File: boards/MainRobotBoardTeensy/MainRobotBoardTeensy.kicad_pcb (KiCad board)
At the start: 2 copper layers, 109.6 x 129.9 mm, 108 parts, among them J1 IDC, J10 B3B-XH-A, J11 B3B-XH-A, J12 B3B-XH-A, J13 B3B-XH-A, J14 IDC, J15 IDC, J16 IDC, J2 B3B-XH-A, J3 B3B-XH-A, J4 B3B-XH-A, J5 B3B-XH-A, J6 B3B-XH-A, J7 B3B-XH-A, J8 B3B-XH-A, J9 B3B-XH-A, Q1 MMBT3904LT1G, Q10 MMBT3904LT1G, Q11 MMBT3904LT1G, Q12 MMBT3904LT1G, Q13 MMBT3904LT1G, Q14 MMBT3904LT1G, Q15 MMBT3904LT1G, Q16 MMBT3904LT1G, Q17 MMBT3904LT1G, Q18 MMBT3904LT1G, Q19 MMBT3904LT1G, Q2 MMBT3904LT1G, Q20 MMBT3904LT1G, Q21 MMBT3904LT1G, Q22 MMBT3904LT1G, Q23 MMBT3904LT1G, Q24 MMBT3904LT1G, Q3 MMBT3904LT1G, Q4 MMBT3904LT1G, Q5 MMBT3904LT1G, Q6 MMBT3904LT1G, Q7 MMBT3904LT1G, Q8 MMBT3904LT1G, Q9 MMBT3904LT1G, U1 Teensy4.0, U2 TLC555CDR, U3 SN74HC08DR, U4 SN74HC08DR, U5 PCA9685PW_118, U6 SN74HC08DR, U7 SN74HC08DR, U8 BNO055

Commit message: Update main and leg board
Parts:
- removed D21, D22, D23, D24: BLUELED, 150080BS75000:150080BS75000_Modified
- removed J15, J16: IDC, Connector_IDC:IDC-Header_2x04_P2.54mm_Vertical
- removed Q21, Q22, Q23, Q24: MMBT3904LT1G, SMMBT3904LT1G:MMBT3904LT1G
- removed U5: PCA9685PW_118, PCA9685PW,118:PCA9685PW,118
- removed U7: SN74HC08DR, SN74HC08DR:SN74HC08DR
- removed U8: BNO055, BNO055:BNO055
- added C5: 47nF, Capacitor47nF:CAPC1608X90N, F.Cu at (110.9, 134.8)
- added C6: 47nF, Capacitor47nF:CAPC1608X90N, F.Cu at (110.9, 137.5)
- added R29: 47R, Resistor47:RESC1608X55, F.Cu at (147.3, 98.9)
- added R30: 47R, Resistor47:RESC1608X55, F.Cu at (141.1, 98.9)
- added R31: 47R, Resistor47:RESC1608X55, F.Cu at (152.6, 105.0)
- added R32: 47R, Resistor47:RESC1608X55, F.Cu at (115.5, 147.5)
- added R33: 47R, Resistor47:RESC1608X55, F.Cu at (152.6, 125.8)
- added R34: 2.2K, Resistor2.2K:RC0603FR-072K2L, F.Cu at (115.4, 129.1)
- added R35: 2.2K, Resistor2.2K:RC0603FR-072K2L, F.Cu at (115.4, 132.0)
- added R36: 2.2K, Resistor2.2K:RC0603FR-072K2L, F.Cu at (115.4, 134.8)
- added R37: 2.2K, Resistor2.2K:RC0603FR-072K2L, F.Cu at (115.4, 137.5)
- added R38: 10K, Resistor10K:CRCW060310K0FKEA, F.Cu at (147.4, 52.3)
- added R39: 10K, Resistor10K:CRCW060310K0FKEA, F.Cu at (152.9, 54.9)
- added R40: 10K, Resistor10K:CRCW060310K0FKEA, F.Cu at (152.9, 70.7)
- added R41: 10K, Resistor10K:CRCW060310K0FKEA, F.Cu at (147.4, 68.1)
- added R42: 10K, Resistor10K:CRCW060310K0FKEA, F.Cu at (152.9, 85.2)
- added R43: 10K, Resistor10K:CRCW060310K0FKEA, F.Cu at (147.4, 81.9)
- added R44: 10K, Resistor10K:CRCW060310K0FKEA, F.Cu at (152.7, 98.9)
- added R45: 10K, Resistor10K:CRCW060310K0FKEA, F.Cu at (141.3, 96.1)
- added R46: 10K, Resistor10K:CRCW060310K0FKEA, F.Cu at (152.7, 107.7)
- added R47: 10K, Resistor10K:CRCW060310K0FKEA, F.Cu at (115.4, 150.1)
- added R48: 10K, Resistor10K:CRCW060310K0FKEA, F.Cu at (141.3, 122.9)
- added R49: 10K, Resistor10K:CRCW060310K0FKEA, F.Cu at (146.7, 143.6)
- added R50: 10K, Resistor10K:CRCW060310K0FKEA, F.Cu at (141.3, 52.3)
- added R51: 10K, Resistor10K:CRCW060310K0FKEA, F.Cu at (141.3, 68.1)
- added R52: 10K, Resistor10K:CRCW060310K0FKEA, F.Cu at (141.3, 82.2)
- added R53: 10K, Resistor10K:CRCW060310K0FKEA, F.Cu at (147.4, 96.1)
- added R54: 10K, Resistor10K:CRCW060310K0FKEA, F.Cu at (95.4, 110.0)
- added R55: 10K, Resistor10K:CRCW060310K0FKEA, F.Cu at (95.4, 134.1)
- added R56: 47R, Resistor47:RESC1608X55, F.Cu at (115.5, 126.4)
- added R57: 47R, Resistor47:RESC1608X55, F.Cu at (141.1, 125.8)
- C1: footprint CC0603JRX7R7BB105:CC0603JRX7R7BB105 -> Capacitor1uF:CC0603JRX7R7BB105
- C2: footprint C0402C103J4RACTU:C0402C103J4RACTU -> Capacitor0.01uF:C0402C103J4RACTU
- C3: value 1uF -> 47nF; footprint CC0603JRX7R7BB105:CC0603JRX7R7BB105 -> Capacitor47nF:CAPC1608X90N
- C4: value 100nF -> 47nF; footprint CC0603KRX7R9BB104:CC0603KRX7R9BB104 -> Capacitor47nF:CAPC1608X90N
- D1, D2, D3, D4, D5, D6, D7, D8: footprint NCD0603R1:NCD0603R1 -> LedRed:NCD0603R1
- D10, D11, D12, D13, D14, D15, D16, D17, D18, D19, D20, D9: footprint 150080BS75000:150080BS75000_Modified -> LedBlue:150080BS75000_Modified
- J1: value IDC -> B3B-XH-A; footprint Connector_IDC:IDC-Header_2x04_P2.54mm_Vertical -> Connector_JST:JST_XH_B3B-XH-A_1x03_P2.50mm_Vertical
- J10, J12: value B3B-XH-A -> B4B-XH-A; footprint Connector_JST:JST_XH_B3B-XH-A_1x03_P2.50mm_Vertical -> Connector_JST:JST_XH_B4B-XH-A_1x04_P2.50mm_Vertical
- J11: value B3B-XH-A -> IDC; footprint Connector_JST:JST_XH_B3B-XH-A_1x03_P2.50mm_Vertical -> Connector_IDC:IDC-Header_2x04_P2.54mm_Vertical
- J13: value B3B-XH-A -> B5B-XH-A; footprint Connector_JST:JST_XH_B3B-XH-A_1x03_P2.50mm_Vertical -> Connector_JST:JST_XH_B5B-XH-A_1x05_P2.50mm_Vertical
- J14: value IDC -> B5B-XH-A; footprint Connector_IDC:IDC-Header_2x04_P2.54mm_Vertical -> Connector_JST:JST_XH_B5B-XH-A_1x05_P2.50mm_Vertical
- Q1, Q10, Q11, Q12, Q13, Q14, Q15, Q16, Q17, Q18, Q19, Q2, Q20, Q3, Q4, Q5, Q6, Q7, Q8, Q9: footprint SMMBT3904LT1G:MMBT3904LT1G -> Transistor:MMBT3904LT1G
- R1: footprint RC0603FR-07360KL:RC0603FR-07360KL -> Resistor360K:RC0603FR-07360KL
- R10, R3, R4, R5, R6, R7, R8, R9: footprint RCG06031K00FKEA:RCG06031K00FKEA -> Resistor1K:RCG06031K00FKEA
- R11, R12, R13, R14, R15, R16, R17, R18, R19, R20, R21, R22: footprint RC0603FR-07150RL:RESC1607X60N -> Resistor150:RESC1607X60N
- R2: footprint CRCW060310K0FKEA:CRCW060310K0FKEA -> Resistor10K:CRCW060310K0FKEA
- R23, R24, R25, R26: value 150R -> 47R; footprint RC0603FR-07150RL:RESC1607X60N -> Resistor47:RESC1608X55
- R27, R28: value 10K -> 47R; footprint CRCW060310K0FKEA:CRCW060310K0FKEA -> Resistor47:RESC1608X55
- U1: footprint Teensy40:Teensy40 -> Teensy:Teensy40
- U2: footprint TLC555CDR:TLC555CDR -> 555Timer:TLC555CDR
- U3, U4, U6: footprint SN74HC08DR:SN74HC08DR -> Gate:SN74HC08DR
- moved J14 111.9 mm to (88.0, 136.1), turned to 90 degrees
- moved J12 104.6 mm to (88.1, 155.5), turned to 90 degrees
- moved D8 99.7 mm to (88.9, 97.2)
- moved D7 95.9 mm to (88.7, 121.4)
- moved J3 94.5 mm to (93.0, 74.3), turned to 180 degrees
- moved J13 93.8 mm to (88.5, 111.3), turned to 90 degrees
- moved C1 90.3 mm to (98.5, 154.1), turned to 90 degrees
- moved U2 85.1 mm to (104.6, 155.5)
- moved R2 84.9 mm to (111.1, 153.4)
- moved R1 84.5 mm to (111.2, 155.6)
- moved C2 84.4 mm to (110.6, 157.8)
- moved R10 77.3 mm to (95.4, 97.0)
- moved Q7 75.3 mm to (96.1, 127.8)
- moved Q8 74.4 mm to (96.1, 103.5)
- moved R9 73.3 mm to (95.4, 121.4)
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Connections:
- net LPWM1BLINK renamed HEADTILT1LPWMBLINK
- net LPWM2BLINK renamed HEADTILT2LPWMBLINK
- net LPWM3BLINK renamed TORSOTILT1LPWMBLINK
- net RPWM1BLINK renamed HEADTILT1RPWMBLINK
- net RPWM2BLINK renamed HEADTILT2RPWMBLINK
- net RPWM3BLINK renamed TORSOTILT1RPWMBLINK
- net RPWM5BLINK renamed TORSOPANPWMBLINK
- C3 pad 1: +3.3V -> Net-(J1-Pin_2)
- C4 pad 1: +3.3V -> Net-(J2-Pin_2)
- J1 pad 2: GND -> Net-(J1-Pin_2)
- J1 pad 3: ENCODER1_A -> GND
- J10 pad 1: PWMEN5 -> +3.3V
- J10 pad 2: RPWM5 -> Net-(J10-Pin_2)
- J10 pad 3: LPWM5 -> HEADPANDIR
- J11 pad 1: PWMEN6 -> TORSOPANEN
- J11 pad 2: RPWM6 -> GND
- J11 pad 3: LPWM6 -> TORSOPANDIR
- J12 pad 1: PWMEN7 -> +3.3V
- J12 pad 2: RPWM7 -> SDA
- J12 pad 3: LPWM7 -> SCL
- J13 pad 1: PWMEN8 -> +3.3V
- J13 pad 2: RPWM8 -> CSHEAD
- J13 pad 3: LPWM8 -> SCK
- J14 pad 2: GND -> CSTORSO
- J14 pad 3: ENCODER2_A -> SCK
- J14 pad 4: GND -> MISO
- J14 pad 5: ENCODER2_B -> GND
- J2 pad 2: A0 -> Net-(J2-Pin_2)
- J3 pad 2: A1 -> Net-(J3-Pin_2)
- J4 pad 2: A2 -> Net-(J4-Pin_2)
- J5 pad 1: +3.3V -> HEADTILT1EN
- J5 pad 2: A3 -> Net-(J5-Pin_2)
- J5 pad 3: GND -> Net-(J5-Pin_3)
- J6 pad 1: PWMEN1 -> HEADTILT2EN
- J6 pad 2: RPWM1 -> Net-(J6-Pin_2)
- J6 pad 3: LPWM1 -> Net-(J6-Pin_3)
- J7 pad 1: PWMEN2 -> TORSOTILT1EN
- J7 pad 2: RPWM2 -> Net-(J7-Pin_2)
- J7 pad 3: LPWM2 -> Net-(J7-Pin_3)
- J8 pad 1: PWMEN3 -> TORSOTILT2EN
- J8 pad 2: RPWM3 -> Net-(J8-Pin_2)
- J8 pad 3: LPWM3 -> Net-(J8-Pin_3)
- J9 pad 1: PWMEN4 -> Net-(J9-Pin_1)
- J9 pad 2: RPWM4 -> +3.3V
- J9 pad 3: LPWM4 -> GND
- Q1 pad 1: PWMEN1 -> HEADTILT1EN
- Q15 pad 1: RPWM4BLINK -> TORSOTILT2RPWMBLINK
- Q16 pad 1: LPWM4BLINK -> TORSOTILT2LPWMBLINK
- Q18 pad 1: LPWM5BLINK -> TORSOPANDIR
- Q19 pad 1: RPWM6BLINK -> HEADPANPUL
- Q2 pad 1: PWMEN2 -> HEADTILT2EN
- Q20 pad 1: LPWM6BLINK -> HEADPANDIR
- Q3 pad 1: PWMEN3 -> TORSOTILT1EN
- Q4 pad 1: PWMEN4 -> TORSOTILT2EN
- Q5 pad 1: PWMEN5 -> TORSOPANEN
- Q6 pad 1: PWMEN6 -> HEADPANEN
- Q7 pad 1: PWMEN7 -> TORSOENCODERST
- Q8 pad 1: PWMEN8 -> HEADENCODERST
- R23 pad 1: Net-(D21-A) -> Net-(J5-Pin_2)
- R23 pad 2: +3.3V -> HEADTILT1RPWM
- R24 pad 1: Net-(D22-A) -> Net-(J5-Pin_3)
- R24 pad 2: +3.3V -> HEADTILT1LPWM
- R25 pad 1: Net-(D23-A) -> Net-(J6-Pin_2)
- R25 pad 2: +3.3V -> HEADTILT2RPWM
- R26 pad 1: Net-(D24-A) -> Net-(J6-Pin_3)
- R26 pad 2: +3.3V -> HEADTILT2LPWM
- R27 pad 1: Net-(U5-*OE) -> Net-(J7-Pin_2)
- R27 pad 2: GND -> TORSOTILT1RPWM
- R28 pad 1: RST -> Net-(J7-Pin_3)
- R28 pad 2: +3.3V -> TORSOTILT1LPWM
- U1 pad 10: ENCODER4_B -> TORSOPANST
- U1 pad 11: PWMEN2 -> TORSOTILT1LPWM
- U1 pad 12: PWMEN3 -> TORSOTILT1RPWM
- U1 pad 13: PWMEN4 -> unconnected-(U1-11_MOSI_CTX1-Pad13)
- U1 pad 14: PWMEN5 -> Net-(U1-12_MISO_MQSL)
- U1 pad 2: ENCODER1_A -> CSHEAD
- U1 pad 20: PWMEN6 -> Net-(U1-13_SCK_CRX1_LED)
- U1 pad 21: A0 -> CURRENT
- U1 pad 22: A1 -> HEAD
- U1 pad 23: A2 -> TORSO1
- U1 pad 24: A3 -> TORSO2
- U1 pad 27: PWMEN7 -> TORSOPANDIR
- U1 pad 28: PWMEN8 -> TORSOPANPWM
- U1 pad 29: ENCODER1_I -> TORSOTILT2LPWM
- U1 pad 3: ENCODER1_B -> CSTORSO
- U1 pad 30: ENCODER2_I -> TORSOTILT2RPWM
- U1 pad 35: ENCODER3_I -> HEADPANPUL
- U1 pad 36: ENCODER4_I -> HEADPANDIR
- U1 pad 37: RST -> MOUTHSERVO
- U1 pad 38: unconnected-(U1-27_A13_SCK1-Pad38) -> HEADTILT1EN
- U1 pad 39: unconnected-(U1-28_RX7-Pad39) -> HEADTILT2EN
- U1 pad 4: ENCODER2_A -> HEADTILT1LPWM
- U1 pad 40: unconnected-(U1-29_TX7-Pad40) -> TORSOTILT1EN
- U1 pad 41: unconnected-(U1-30_CRX3-Pad41) -> TORSOTILT2EN
- U1 pad 5: ENCODER2_B -> HEADTILT1RPWM
- U1 pad 6: ENCODER3_A -> HEADTILT2LPWM
- U1 pad 7: ENCODER3_B -> HEADTILT2RPWM
- U1 pad 8: PWMEN1 -> HEADPANEN
- U1 pad 9: ENCODER4_A -> TORSOPANEN
- U3 pad 10: RPWM2 -> HEADTILT2RPWM
- U3 pad 13: LPWM2 -> HEADTILT2LPWM
- U3 pad 2: RPWM1 -> HEADTILT1RPWM
- U3 pad 5: LPWM1 -> HEADTILT1LPWM
- U4 pad 10: LPWM4 -> TORSOTILT2RPWM
- U4 pad 11: RPWM4BLINK -> TORSOTILT2LPWMBLINK
- U4 pad 13: RPWM4 -> TORSOTILT2LPWM
- U4 pad 2: RPWM3 -> TORSOTILT1RPWM
- U4 pad 5: LPWM3 -> TORSOTILT1LPWM
- U4 pad 8: LPWM4BLINK -> TORSOTILT2RPWMBLINK
- U6 pad 10: LPWM6 -> unconnected-(U6-3B-Pad10)
- U6 pad 11: RPWM6BLINK -> unconnected-(U6-4Y-Pad11)
- U6 pad 12: BLINK -> unconnected-(U6-4A-Pad12)
- U6 pad 13: RPWM6 -> unconnected-(U6-4B-Pad13)
- U6 pad 2: RPWM5 -> TORSOPANPWM
- U6 pad 4: BLINK -> unconnected-(U6-2A-Pad4)
- U6 pad 5: LPWM5 -> unconnected-(U6-2B-Pad5)
- U6 pad 6: LPWM5BLINK -> unconnected-(U6-2Y-Pad6)
- U6 pad 8: LPWM6BLINK -> unconnected-(U6-3Y-Pad8)
- U6 pad 9: BLINK -> unconnected-(U6-3A-Pad9)
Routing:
- net HEADTILT2LPWM: track 0.00 -> 176.1 mm, vias 0 -> 4
- net HEADTILT1LPWM: track 0.00 -> 175.7 mm, vias 0 -> 4
- net HEADTILT2RPWM: track 0.00 -> 170.6 mm, vias 0 -> 4
- net TORSOTILT2RPWM: track 0.00 -> 166.1 mm, vias 0 -> 4
- net HEADTILT1EN: track 0.00 -> 164.3 mm, vias 0 -> 3
- net TORSOTILT1LPWM: track 0.00 -> 140.8 mm, vias 0 -> 4
- net HEADTILT1RPWM: track 0.00 -> 138.6 mm, vias 0 -> 4
- net PWMEN1: track 138.4 -> 0.00 mm, vias 2 -> 0
- net TORSOTILT1EN: track 0.00 -> 134.9 mm, vias 0 -> 3
- net A1: track 125.1 -> 0.00 mm, vias 1 -> 0
- net HEADTILT2EN: track 0.00 -> 123.8 mm, vias 0 -> 7
- net ENCODER1_B: track 117.0 -> 0.00 mm, vias 1 -> 0
- net ENCODER2_I: track 110.6 -> 0.00 mm, vias 1 -> 0
- net PWMEN2: track 109.3 -> 0.00 mm, vias 2 -> 0
- net A0: track 108.9 -> 0.00 mm, vias 1 -> 0
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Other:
- board size 109.6 x 129.9 mm -> 107 x 129 mm
- board text added: "A0"
- board text added: "A1"
- board text added: "A2"
- board text added: "A3"
- board text added: "Actuators"
- board text added: "CURRENT"
- board text added: "D0"
- board text added: "D1"
- board text added: "D2/D3"
- board text added: "D20/21"
- board text added: "D22/23"
- board text added: "D24/25"
- board text added: "D26"
- board text added: "D27"
- board text added: "D28"
- board text added: "D29"
- board text added: "D30"
- board text added: "D4/D5"
- board text added: "D6"
- board text added: "D7"
- board text added: "D9/10"
- board text added: "DIR PWM"
- board text added: "HEAD PAN"
- board text added: "HEAD TILT"
- board text added: "HEAD TILT 1"
- board text added: "HEAD TILT 2"
- board text added: "I2C"
- board text added: "MOUTH"
- board text added: "PUL DIR"
- board text added: "SPI"
- board text added: "Sensors"
- board text added: "TORSO PAN"
- board text added: "TORSO TILT 1"
- board text added: "TORSO TILT 2"
- board text added: "VOLTAGE"
- board text removed: "ABI1"
- board text removed: "ABI2"
- board text removed: "ABI3"
- board text removed: "ABI4"
- board text removed: "ADC0"
- board text removed: "ADC1"
- board text removed: "ADC2"
- board text removed: "ADC3"
- board text removed: "BACK LEFT"
- board text removed: "BACK RIGHT"
- board text removed: "FRONT LEFT"
- board text removed: "FRONT RIGHT"
- board text removed: "MOBILE PLATFORM"
- board text removed: "PWM1"
- board text removed: "PWM2"
- board text removed: "PWM3"
- board text removed: "PWM4"
- board text removed: "PWM5"
- board text removed: "PWM6"
- board text removed: "PWM7"
- board text removed: "PWM8"

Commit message: Add OLED display, light bar, voltage and current sensors
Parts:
- removed J1: B3B-XH-A, Connector_JST:JST_XH_B3B-XH-A_1x03_P2.50mm_Vertical
- removed J12: B4B-XH-A, Connector_JST:JST_XH_B4B-XH-A_1x04_P2.50mm_Vertical
- added C7: 100nF, Capacitor100nF:CC0603KRX7R9BB104, F.Cu at (113.0, 136.0)
- added C8: 100nF, Capacitor100nF:CC0603KRX7R9BB104, F.Cu at (113.0, 133.4)
- added R100: 150R, Resistor150:RESC1607X60N, F.Cu at (108.8, 138.5)
- added R101: 150R, Resistor150:RESC1607X60N, F.Cu at (108.8, 141.0)
- added R102: 150R, Resistor150:RESC1607X60N, F.Cu at (108.8, 143.6)
- added R103: 150R, Resistor150:RESC1607X60N, F.Cu at (108.8, 146.2)
- added R104: 150R, Resistor150:RESC1607X60N, F.Cu at (108.8, 148.7)
- added R105: 150R, Resistor150:RESC1607X60N, F.Cu at (108.8, 151.2)
- added R106: 150R, Resistor150:RESC1607X60N, F.Cu at (108.8, 153.8)
- added R107: 150R, Resistor150:RESC1607X60N, F.Cu at (108.8, 156.4)
- added R58: 10K, Resistor10K:CRCW060310K0FKEA, F.Cu at (78.4, 113.2)
- added R59: 100K, Resistor100K:CRCW0603100KFKEA, F.Cu at (78.4, 115.8)
- added R60: 10K, Resistor10K:CRCW060310K0FKEA, F.Cu at (100.4, 113.2)
- added R61: 100K, Resistor100K:CRCW0603100KFKEA, F.Cu at (100.4, 115.8)
- added R62: 10K, Resistor10K:CRCW060310K0FKEA, F.Cu at (122.6, 113.2)
- added R63: 100K, Resistor100K:CRCW0603100KFKEA, F.Cu at (122.6, 115.8)
- added R64: 10K, Resistor10K:CRCW060310K0FKEA, F.Cu at (144.4, 113.2)
- added R65: 100K, Resistor100K:CRCW0603100KFKEA, F.Cu at (144.4, 115.8)
- added R66: 10K, Resistor10K:CRCW060310K0FKEA, F.Cu at (188.5, 113.3)
- added R67: 100K, Resistor100K:CRCW0603100KFKEA, F.Cu at (188.5, 115.8)
- added R68: 10K, Resistor10K:CRCW060310K0FKEA, F.Cu at (166.5, 113.1)
- added R69: 100K, Resistor100K:CRCW0603100KFKEA, F.Cu at (166.5, 115.8)
- added R70: 10K, Resistor10K:CRCW060310K0FKEA, F.Cu at (208.2, 75.3)
- added R71: 100K, Resistor100K:CRCW0603100KFKEA, F.Cu at (208.2, 77.5)
- added R72: 10K, Resistor10K:CRCW060310K0FKEA, F.Cu at (208.2, 69.6)
- added R73: 100K, Resistor100K:CRCW0603100KFKEA, F.Cu at (208.2, 71.8)
- added R74: 10K, Resistor10K:CRCW060310K0FKEA, F.Cu at (84.4, 113.2)
- added R75: 100K, Resistor100K:CRCW0603100KFKEA, F.Cu at (84.4, 115.8)
- added R76: 10K, Resistor10K:CRCW060310K0FKEA, F.Cu at (72.5, 113.2)
- added R77: 100K, Resistor100K:CRCW0603100KFKEA, F.Cu at (72.5, 115.8)
- added R78: 10K, Resistor10K:CRCW060310K0FKEA, F.Cu at (106.4, 113.2)
- added R79: 100K, Resistor100K:CRCW0603100KFKEA, F.Cu at (106.4, 115.8)
- added R80: 10K, Resistor10K:CRCW060310K0FKEA, F.Cu at (94.5, 113.2)
- added R81: 100K, Resistor100K:CRCW0603100KFKEA, F.Cu at (94.5, 115.8)
- added R82: 10K, Resistor10K:CRCW060310K0FKEA, F.Cu at (128.8, 113.2)
- added R83: 100K, Resistor100K:CRCW0603100KFKEA, F.Cu at (128.8, 115.8)
- added R84: 10K, Resistor10K:CRCW060310K0FKEA, F.Cu at (116.5, 113.2)
- added R85: 100K, Resistor100K:CRCW0603100KFKEA, F.Cu at (116.5, 115.8)
- added R86: 10K, Resistor10K:CRCW060310K0FKEA, F.Cu at (150.7, 113.1)
- added R87: 100K, Resistor100K:CRCW0603100KFKEA, F.Cu at (150.7, 115.8)
- added R88: 10K, Resistor10K:CRCW060310K0FKEA, F.Cu at (138.4, 113.2)
- added R89: 100K, Resistor100K:CRCW0603100KFKEA, F.Cu at (138.4, 115.8)
- added R90: 10K, Resistor10K:CRCW060310K0FKEA, F.Cu at (182.3, 113.3)
- added R91: 100K, Resistor100K:CRCW0603100KFKEA, F.Cu at (182.3, 115.8)
- added R92: 10K, Resistor10K:CRCW060310K0FKEA, F.Cu at (194.6, 113.3)
- added R93: 100K, Resistor100K:CRCW0603100KFKEA, F.Cu at (194.6, 115.8)
- added R94: 10K, Resistor10K:CRCW060310K0FKEA, F.Cu at (160.4, 113.1)
- added R95: 100K, Resistor100K:CRCW0603100KFKEA, F.Cu at (160.4, 115.8)
- added R96: 10K, Resistor10K:CRCW060310K0FKEA, F.Cu at (172.7, 113.1)
- added R97: 100K, Resistor100K:CRCW0603100KFKEA, F.Cu at (172.7, 115.8)
- added R98: 150R, Resistor150:RESC1607X60N, F.Cu at (108.8, 133.4)
- added R99: 150R, Resistor150:RESC1607X60N, F.Cu at (108.8, 136.0)
- added U10: KWL-R1025BB, LedBar:KWL-R1025BB, F.Cu at (101.8, 144.9)
- added U11: SSD1306, SSD1306:SSD1306, F.Cu at (131.0, 144.0)
- added U5: INA260, INA260:INA260, F.Cu at (81.8, 145.9)
- added U7: ACS37220, ACS37220:ACS37220, F.Cu at (202.3, 142.4)
- added U8: D0016A_N, ShiftRegister:SN74HC595DR, F.Cu at (85.9, 124.0)
- added U9: D0016A_N, ShiftRegister:SN74HC595DR, F.Cu at (107.9, 124.0)
- Q1, Q10, Q11, Q12, Q13, Q14, Q15, Q16, Q17, Q18, Q19, Q2, Q20, Q3, Q4, Q5, Q6, Q7, Q8, Q9: value MMBT3904LT1G -> AO3400A; footprint Transistor:MMBT3904LT1G -> AO3400A:AO3400A
- moved R55 138.9 mm to (221.2, 75.3)
- moved R9 133.3 mm to (221.2, 77.5)
- moved R54 132.1 mm to (221.2, 69.6)
- moved Q7 129.4 mm to (214.9, 76.4)
- moved R10 128.3 mm to (221.2, 71.8)
- moved J14 125.9 mm to (198.4, 75.4), turned to 180 degrees
- moved Q8 122.9 mm to (214.6, 70.7)
- moved D7 112.5 mm to (193.4, 80.1)
- moved D1 101.8 mm to (76.0, 101.0)
- moved D9 101.8 mm to (79.4, 101.0)
- moved D10 101.8 mm to (72.6, 101.0)
- moved R38 100.1 mm to (182.2, 146.2)
- moved R11 99.5 mm to (72.5, 105.7)
- moved R24 98.6 mm to (177.8, 148.6), turned to 180 degrees
- moved R23 98.4 mm to (177.8, 146.2), turned to 180 degrees
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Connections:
- Q1 pad 1: HEADTILT1EN -> Net-(Q1-Pad1)
- Q1 pad 2: GND -> Net-(D1-K)
- Q1 pad 3: Net-(D1-K) -> GND
- Q10 pad 1: HEADTILT1LPWMBLINK -> Net-(Q10-Pad1)
- Q10 pad 2: GND -> Net-(D10-K)
- Q10 pad 3: Net-(D10-K) -> GND
- Q11 pad 1: HEADTILT2RPWMBLINK -> Net-(Q11-Pad1)
- Q11 pad 2: GND -> Net-(D11-K)
- Q11 pad 3: Net-(D11-K) -> GND
- Q12 pad 1: HEADTILT2LPWMBLINK -> Net-(Q12-Pad1)
- Q12 pad 2: GND -> Net-(D12-K)
- Q12 pad 3: Net-(D12-K) -> GND
- Q13 pad 1: TORSOTILT1RPWMBLINK -> Net-(Q13-Pad1)
- Q13 pad 2: GND -> Net-(D13-K)
- Q13 pad 3: Net-(D13-K) -> GND
- Q14 pad 1: TORSOTILT1LPWMBLINK -> Net-(Q14-Pad1)
- Q14 pad 2: GND -> Net-(D14-K)
- Q14 pad 3: Net-(D14-K) -> GND
- Q15 pad 1: TORSOTILT2RPWMBLINK -> Net-(Q15-Pad1)
- Q15 pad 2: GND -> Net-(D15-K)
- Q15 pad 3: Net-(D15-K) -> GND
- Q16 pad 1: TORSOTILT2LPWMBLINK -> Net-(Q16-Pad1)
- Q16 pad 2: GND -> Net-(D16-K)
- Q16 pad 3: Net-(D16-K) -> GND
- Q17 pad 1: TORSOPANPWMBLINK -> Net-(Q17-Pad1)
- Q17 pad 2: GND -> Net-(D17-K)
- Q17 pad 3: Net-(D17-K) -> GND
- Q18 pad 1: TORSOPANDIR -> Net-(Q18-Pad1)
- Q18 pad 2: GND -> Net-(D18-K)
- Q18 pad 3: Net-(D18-K) -> GND
- Q19 pad 1: HEADPANPUL -> Net-(Q19-Pad1)
- Q19 pad 2: GND -> Net-(D19-K)
- Q19 pad 3: Net-(D19-K) -> GND
- Q2 pad 1: HEADTILT2EN -> Net-(Q2-Pad1)
- Q2 pad 2: GND -> Net-(D2-K)
- Q2 pad 3: Net-(D2-K) -> GND
- Q20 pad 1: HEADPANDIR -> Net-(Q20-Pad1)
- Q20 pad 2: GND -> Net-(D20-K)
- Q20 pad 3: Net-(D20-K) -> GND
- Q3 pad 1: TORSOTILT1EN -> Net-(Q3-Pad1)
- Q3 pad 2: GND -> Net-(D3-K)
- Q3 pad 3: Net-(D3-K) -> GND
- Q4 pad 1: TORSOTILT2EN -> Net-(Q4-Pad1)
- Q4 pad 2: GND -> Net-(D4-K)
- Q4 pad 3: Net-(D4-K) -> GND
- Q5 pad 1: TORSOPANEN -> Net-(Q5-Pad1)
- Q5 pad 2: GND -> Net-(D5-K)
- Q5 pad 3: Net-(D5-K) -> GND
- Q6 pad 1: HEADPANEN -> Net-(Q6-Pad1)
- Q6 pad 2: GND -> Net-(D6-K)
- Q6 pad 3: Net-(D6-K) -> GND
- Q7 pad 1: TORSOENCODERST -> Net-(Q7-Pad1)
- Q7 pad 2: GND -> Net-(D7-K)
- Q7 pad 3: Net-(D7-K) -> GND
- Q8 pad 1: HEADENCODERST -> Net-(Q8-Pad1)
- Q8 pad 2: GND -> Net-(D8-K)
- Q8 pad 3: Net-(D8-K) -> GND
- Q9 pad 1: HEADTILT1RPWMBLINK -> Net-(Q9-Pad1)
- Q9 pad 2: GND -> Net-(D9-K)
- Q9 pad 3: Net-(D9-K) -> GND
- U1 pad 13: unconnected-(U1-11_MOSI_CTX1-Pad13) -> MOSI
- U1 pad 42: unconnected-(U1-31_CTX3-Pad42) -> RCLK1
- U1 pad 43: unconnected-(U1-32_OUT1B-Pad43) -> RCLK2
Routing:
- net Net-(J5-Pin_3): track 16.3 -> 159.9 mm, vias 0 -> 2
- net +3.3V: track 575.3 -> 711.9 mm
- net Net-(J5-Pin_2): track 26.4 -> 156.4 mm, vias 1 -> 2
- net RCLK1: track 0.00 -> 124.9 mm, vias 0 -> 5
- net SCK: track 55.6 -> 166.3 mm, vias 1 -> 4
- net Net-(J6-Pin_2): track 19.0 -> 126.4 mm, vias 0 -> 2
- net MOSI: track 0.00 -> 106.5 mm, vias 0 -> 6
- net Net-(J6-Pin_3): track 23.2 -> 128.7 mm, vias 1 -> 3
- net TORSOTILT2RPWM: track 166.1 -> 81.1 mm, vias 4 -> 2
- net Net-(J7-Pin_3): track 23.7 -> 99.2 mm, vias 1 -> 2
- net Net-(J7-Pin_2): track 19.1 -> 90.7 mm, vias 0 -> 2
- net RCLK2: track 0.00 -> 65.5 mm, vias 0 -> 2
- net Net-(D8-A): track 5.18 -> 70.2 mm
- net BLINK: track 167.6 -> 104.4 mm, vias 2 -> 7
- net SCL: track 35.6 -> 98.4 mm, vias 0 -> 2
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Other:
- board size 107 x 129 mm -> 174 x 121.1 mm
- board text added: "ACS37220"
- board text added: "ANALOG"
- board text added: "BATTERY LEVEL"
- board text added: "CURRENT SENSOR"
- board text added: "DIGITAL"
- board text added: "MOTORS"
- board text added: "OLED DISPLAY"
- board text added: "SERVOS AND STEPPERS"
- board text added: "SSD1306"
- board text added: "actuators"
- board text added: "sensors"
- board text removed: "A0"
- board text removed: "Actuators"
- board text removed: "I2C"
- board text removed: "SPI"
- board text removed: "Sensors"

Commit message: Finalize main robot board
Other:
- board text added: "+"
- board text added: "-"
- board text added: "01 BINARY TECH ART"
- board text removed: "CURRENT"
- board text removed: "CURRENT SENSOR"
- board text removed: "VOLTAGE"

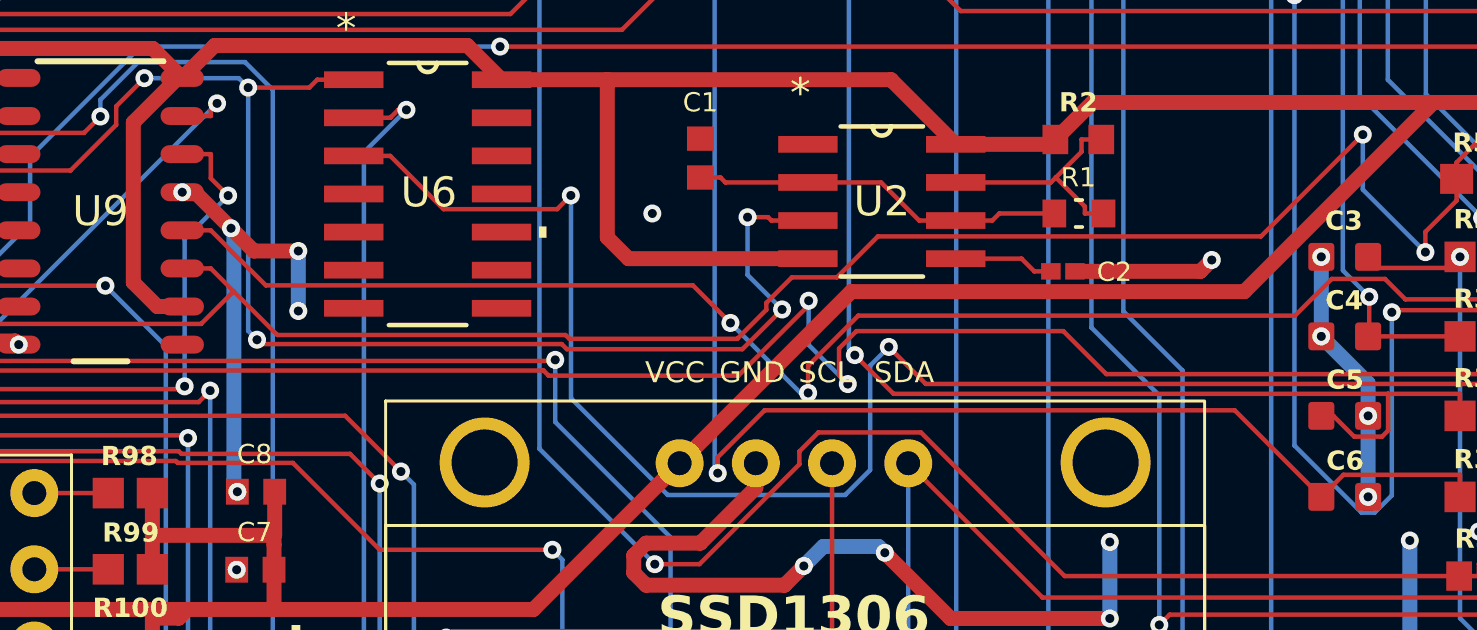
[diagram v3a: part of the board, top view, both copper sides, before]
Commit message: Re-routing main board, found a mistake
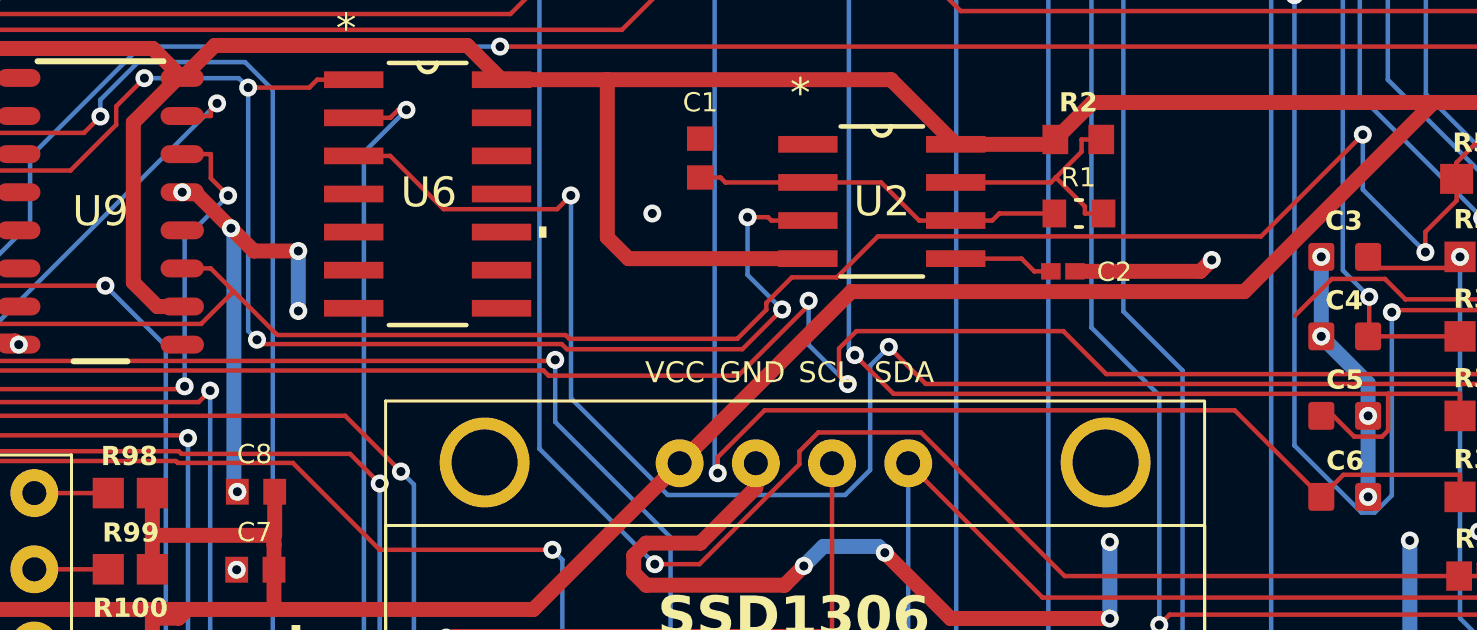
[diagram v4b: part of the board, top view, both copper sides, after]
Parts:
- U8, U9: value D0016A_N -> SN74HC595DR
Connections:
- U1 pad 42: RCLK1 -> RCLK
- U1 pad 43: RCLK2 -> unconnected-(U1-32_OUT1B-Pad43)
- U8 pad 12: RCLK1 -> RCLK
- U9 pad 12: RCLK2 -> RCLK
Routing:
- net RCLK1: track 124.9 -> 0.00 mm, vias 5 -> 0
- net RCLK: track 0.00 -> 124.9 mm, vias 0 -> 5
- net RCLK2: track 65.5 -> 0.00 mm, vias 2 -> 0
- net unconnected-(U1-32_OUT1B-Pad43): track 0.00 -> 24.6 mm
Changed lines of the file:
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@@
 	(net 155 "Net-(U10-LED10+)")
 	(net 156 "MOSI")
-	(net 157 "RCLK2")
-	(net 158 "RCLK1")
+	(net 157 "unconnected-(U1-32_OUT1B-Pad43)")
+	(net 158 "RCLK")
 	(net 159 "LED7")
 	(net 160 "LED8")
@@
 			)
 		)
-		(property "Value" "D0016A_N"
+		(property "Value" "SN74HC595DR"
 			(at 0 0 0)
 			(unlocked yes)
@@
 			(size 0.599999 1.45)
 			(layers "F.Cu" "F.Mask" "F.Paste")
-			(net 158 "RCLK1")
+			(net 158 "RCLK")
 			(pinfunction "RCLK")
 			(pintype "input")
@@
 		(sheetname "/")
 		(sheetfile "MainRobotBoardTeensy.kicad_sch")
-		(attr smd exclude_from_pos_files exclude_from_bom)
+		(attr smd exclude_from_pos_files)
 		(fp_rect
 			(start -12.75 -5.05)
@@
 		(sheetname "/")
 		(sheetfile "MainRobotBoardTeensy.kicad_sch")
-		(attr through_hole exclude_from_pos_files exclude_from_bom)
+		(attr through_hole exclude_from_pos_files)
 		(fp_line
 			(start 5.83 -5.21)
@@
 			)
 		)
-		(property "Value" "D0016A_N"
+		(property "Value" "SN74HC595DR"
 			(at 0 0 0)
 			(unlocked yes)
@@
 			(size 0.599999 1.45)
 			(layers "F.Cu" "F.Mask" "F.Paste")
-			(net 157 "RCLK2")
+			(net 158 "RCLK")
 			(pinfunction "RCLK")
 			(pintype "input")
@@
 		(sheetname "/")
 		(sheetfile "MainRobotBoardTeensy.kicad_sch")
-		(attr through_hole exclude_from_pos_files exclude_from_bom)
+		(attr through_hole exclude_from_pos_files)
 		(fp_line
 			(start 10.06 3.51)
@@
 		(sheetname "/")
 		(sheetfile "MainRobotBoardTeensy.kicad_sch")
-		(attr smd exclude_from_pos_files exclude_from_bom)
+		(attr smd exclude_from_pos_files)
 		(fp_rect
 			(start -13.65 -13.65)
@@
 		(sheetname "/")
 		(sheetfile "MainRobotBoardTeensy.kicad_sch")
-		(attr smd exclude_from_pos_files exclude_from_bom)
+		(attr smd exclude_from_pos_files)
 		(fp_line
 			(start -11.29 -8.3468)
@@
 		(sheetname "/")
 		(sheetfile "MainRobotBoardTeensy.kicad_sch")
-		(attr through_hole exclude_from_pos_files exclude_from_bom)
+		(attr through_hole exclude_from_pos_files)
 		(fp_line
 			(start 12.56 3.51)
@@
 		(sheetname "/")
 		(sheetfile "MainRobotBoardTeensy.kicad_sch")
-		(attr through_hole exclude_from_pos_files exclude_from_bom)
+		(attr through_hole exclude_from_pos_files)
 		(fp_line
 			(start 17.78 -8.89)
@@
 			(layers "*.Cu" "*.Mask")
 			(remove_unused_layers no)
-			(net 158 "RCLK1")
+			(net 158 "RCLK")
 			(pinfunction "31_CTX3")
 			(pintype "bidirectional")
@@
 			(layers "*.Cu" "*.Mask")
 			(remove_unused_layers no)
-			(net 157 "RCLK2")
+			(net 157 "unconnected-(U1-32_OUT1B-Pad43)")
 			(pinfunction "32_OUT1B")
-			(pintype "bidirectional")
+			(pintype "bidirectional+no_connect")
 		)
 		(pad "44" thru_hole circle
@@
 		(sheetname "/")
 		(sheetfile "MainRobotBoardTeensy.kicad_sch")
-		(attr smd exclude_from_bom)
+		(attr smd)
 		(fp_rect
 			(start 17.8 -15.25)
@@
 		(sheetname "/")
 		(sheetfile "MainRobotBoardTeensy.kicad_sch")
-		(attr through_hole exclude_from_pos_files exclude_from_bom)
+		(attr through_hole exclude_from_pos_files)
 		(fp_line
 			(start 12.56 3.51)
@@
 	)
 	(segment
-		(start 110.581 124.661)
-		(end 111.5327 124.661)
-		(width 0.15)
-		(layer "F.Cu")
-		(net 157)
-	)
-	(segment
 		(start 150.6724 126.2812)
 		(end 151.3528 126.9616)
@@
 	)
 	(segment
-		(start 131.4434 130.0813)
-		(end 131.4434 129.1763)
-		(width 0.15)
-		(layer "F.Cu")
-		(net 157)
-	)
-	(segment
-		(start 131.4434 129.1763)
-		(end 133.1143 127.5054)
-		(width 0.15)
-		(layer "F.Cu")
-		(net 157)
-	)
-	(segment
-		(start 127.6023 126.4961)
-		(end 128.8544 127.7482)
-		(width 0.15)
-		(layer "F.Cu")
-		(net 157)
-	)
-	(segment
-		(start 111.5327 124.661)
-		(end 113.3678 126.4961)
-		(width 0.15)
-		(layer "F.Cu")
-		(net 157)
-	)
-	(segment
 		(start 169.395 126.9616)
 		(end 170.8394 128.406)
@@
 	)
 	(segment
-		(start 133.1143 127.5054)
-		(end 147.6726 127.5054)
-		(width 0.15)
-		(layer "F.Cu")
-		(net 157)
-	)
-	(segment
 		(start 147.6726 127.5054)
 		(end 148.8968 126.2812)
@@
 		(net 157)
 	)
-	(segment
-		(start 113.3678 126.4961)
-		(end 127.6023 126.4961)
-		(width 0.15)
-		(layer "F.Cu")
-		(net 157)
-	)
-	(via
-		(at 131.4434 130.0813)
-		(size 0.6)
-		(drill 0.3)
-		(layers "F.Cu" "B.Cu")
-		(net 157)
-	)
-	(via
-		(at 128.8544 127.7482)
-		(size 0.6)
-		(drill 0.3)
-		(layers "F.Cu" "B.Cu")
-		(net 157)
-	)
-	(segment
-		(start 131.1875 130.0813)
-		(end 131.4434 130.0813)
-		(width 0.15)
-		(layer "B.Cu")
-		(net 157)
-	)
-	(segment
-		(start 128.8544 127.7482)
-		(end 131.1875 130.0813)
-		(width 0.15)
-		(layer "B.Cu")
-		(net 157)
-	)

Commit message: Finalize main board
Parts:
- removed C1: 1uF, Capacitor1uF:CC0603JRX7R7BB105
- removed C2: 0.01uF, Capacitor0.01uF:C0402C103J4RACTU
- removed R1: 360K, Resistor360K:RC0603FR-07360KL
- removed R2: 10K, Resistor10K:CRCW060310K0FKEA
- removed R59, R61, R63, R65, R67, R69: 100K, Resistor100K:CRCW0603100KFKEA
- removed U2: TLC555CDR, 555Timer:TLC555CDR
- U8, U9: value SN74HC595DR -> D0016A_N
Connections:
- U9 pad 2: unconnected-(U9-QC-Pad2) -> TORSOENCODERST
- U9 pad 3: unconnected-(U9-QD-Pad3) -> HEADENCODERST
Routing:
- net HEADENCODERST: track 2.12 -> 150.3 mm, vias 0 -> 2
- net TORSOENCODERST: track 2.12 -> 147.7 mm, vias 0 -> 2
- net BLINK: track 104.4 -> 72.1 mm, vias 7 -> 4
- net unconnected-(U1-32_OUT1B-Pad43): track 24.6 -> 0.00 mm
- net +3.3V: track 711.9 -> 698.6 mm
- net /NODE_A: track 12.5 -> 0.00 mm
- net RCLK: track 124.9 -> 134.1 mm, vias 5 -> 7
- net /NODE_B: track 7.91 -> 0.00 mm
- net GND: track 137.8 -> 133.1 mm, vias 93 -> 94
- net Net-(U2-CONT): track 3.35 -> 0.00 mm
- net HEADTILT1EN: track 139.5 -> 136.6 mm
- net TORSOTILT1EN: track 93.5 -> 90.8 mm
- net HEADTILT2EN: track 118.7 -> 116.0 mm
